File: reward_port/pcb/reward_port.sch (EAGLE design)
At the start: 27 parts

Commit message: initial routing
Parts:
- removed J3: (no value), SparkFun-Connectors:M05X2PTH
- added INDICATOR_LED: (no value), SparkFun-LED:LED-3MM-NO_SILK
- added R8: 270, SparkFun-Resistors:10KOHM-1/10W-1%(0603)0603
- R6: value 100 -> 270
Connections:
- removed net N$20: J3.7, U$6.PB7
- removed net N$22: J3.5, U$6.PB6(ADC13)
- removed net N$23: J3.3, U$6.PB5(ADC12)
- removed net N$24: J3.1, U$6.PB4(ADC11)
- removed net N$25: J3.2, U$6.PE6
- removed net N$26: J3.4, U$6.PD7(ADC10)
- removed net N$27: J3.6, U$6.PC6
- removed net N$3: J3.9, U$6.PD6(ADC9)
- new net INDICATOR_OUT: INDICATOR_LED.A, U$6.PC6
- new net N$10: U$6.PB7
- new net N$14: U$6.PD6(ADC9)
- new net N$16: INDICATOR_LED.C, R8.2
- new net N$4: U$6.PD7(ADC10)
- new net N$5: U$6.PB6(ADC13)
- net GND: now also R8.1; no longer J3.8
- net VDD: no longer J3.10
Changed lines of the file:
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@@
 <part name="C3" library="SparkFun-Capacitors" deviceset="10UF-6.3V-20%(0603)" device="" value="10uF"/>
 <part name="C4" library="SparkFun-Capacitors" deviceset="0.1UF-25V-5%(0603)" device="" value="0.1uF"/>
-<part name="J3" library="SparkFun-Connectors" deviceset="M05X2" device="PTH"/>
-<part name="R6" library="SparkFun-Resistors" deviceset="10KOHM-1/10W-1%(0603)" device="0603" value="100"/>
+<part name="R6" library="SparkFun-Resistors" deviceset="10KOHM-1/10W-1%(0603)" device="0603" value="270"/>
 <part name="GND12" library="supply1" deviceset="GND" device=""/>
 <part name="GND13" library="supply1" deviceset="GND" device=""/>
 <part name="R7" library="SparkFun-Resistors" deviceset="10KOHM-1/10W-1%(0603)" device="0603" value="100"/>
 <part name="J7" library="SparkFun-Connectors" deviceset="M04" device="POLAR"/>
+<part name="INDICATOR_LED" library="SparkFun-LED" deviceset="LED" device="-3MM-NO_SILK"/>
+<part name="R8" library="SparkFun-Resistors" deviceset="10KOHM-1/10W-1%(0603)" device="0603" value="270"/>
 <part name="GND14" library="supply1" deviceset="GND" device=""/>
 </parts>
@@
 <instance part="C3" gate="G$1" x="408.94" y="411.48"/>
 <instance part="C4" gate="G$1" x="388.62" y="411.48"/>
-<instance part="J3" gate="G$1" x="391.16" y="266.7"/>
 <instance part="R6" gate="G$1" x="469.9" y="256.54" rot="R90"/>
 <instance part="GND12" gate="1" x="469.9" y="246.38" rot="MR0"/>
@@
 <instance part="R7" gate="G$1" x="492.76" y="281.94" rot="R180"/>
 <instance part="J7" gate="G$1" x="403.86" y="368.3" rot="R180"/>
-<instance part="GND14" gate="1" x="414.02" y="264.16" rot="MR270"/>
+<instance part="INDICATOR_LED" gate="G$1" x="454.66" y="269.24"/>
+<instance part="R8" gate="G$1" x="454.66" y="256.54" rot="R90"/>
+<instance part="GND14" gate="1" x="454.66" y="246.38" rot="MR0"/>
 </instances>
 <busses>
@@
 </segment>
 <segment>
-<pinref part="J3" gate="G$1" pin="8"/>
 <pinref part="GND14" gate="1" pin="GND"/>
-<wire x1="411.48" y1="264.16" x2="398.78" y2="264.16" width="0.1524" layer="91"/>
+<pinref part="R8" gate="G$1" pin="1"/>
+<wire x1="454.66" y1="248.92" x2="454.66" y2="251.46" width="0.1524" layer="91"/>
 </segment>
 </net>
@@
 <wire x1="497.84" y1="281.94" x2="502.92" y2="281.94" width="0.1524" layer="91"/>
 <label x="505.46" y="284.48" size="1.778" layer="95"/>
-</segment>
-<segment>
-<pinref part="J3" gate="G$1" pin="10"/>
-<wire x1="398.78" y1="261.62" x2="401.32" y2="261.62" width="0.1524" layer="91"/>
-<label x="401.32" y="261.62" size="1.778" layer="95"/>
 </segment>
 </net>
@@
 <wire x1="469.9" y1="264.16" x2="469.9" y2="261.62" width="0.1524" layer="91"/>
 <pinref part="R6" gate="G$1" pin="2"/>
-</segment>
-</net>
-<net name="N$3" class="0">
+<wire x1="469.9" y1="266.7" x2="469.9" y2="264.16" width="0.1524" layer="91"/>
+</segment>
+</net>
+<net name="N$5" class="0">
+<segment>
+<pinref part="U$6" gate="G$1" pin="PB6(ADC13)"/>
+<wire x1="378.46" y1="266.7" x2="383.54" y2="266.7" width="0.1524" layer="91"/>
+</segment>
+</net>
+<net name="N$10" class="0">
+<segment>
+<pinref part="U$6" gate="G$1" pin="PB7"/>
+<wire x1="378.46" y1="264.16" x2="383.54" y2="264.16" width="0.1524" layer="91"/>
+</segment>
+</net>
+<net name="N$14" class="0">
 <segment>
 <pinref part="U$6" gate="G$1" pin="PD6(ADC9)"/>
-<pinref part="J3" gate="G$1" pin="9"/>
-<wire x1="383.54" y1="261.62" x2="378.46" y2="261.62" width="0.1524" layer="91"/>
-</segment>
-</net>
-<net name="N$20" class="0">
-<segment>
-<pinref part="U$6" gate="G$1" pin="PB7"/>
-<pinref part="J3" gate="G$1" pin="7"/>
-<wire x1="383.54" y1="264.16" x2="378.46" y2="264.16" width="0.1524" layer="91"/>
-</segment>
-</net>
-<net name="N$22" class="0">
-<segment>
-<pinref part="U$6" gate="G$1" pin="PB6(ADC13)"/>
-<pinref part="J3" gate="G$1" pin="5"/>
-<wire x1="383.54" y1="266.7" x2="378.46" y2="266.7" width="0.1524" layer="91"/>
-</segment>
-</net>
-<net name="N$23" class="0">
-<segment>
-<pinref part="U$6" gate="G$1" pin="PB5(ADC12)"/>
-<pinref part="J3" gate="G$1" pin="3"/>
-<wire x1="383.54" y1="269.24" x2="378.46" y2="269.24" width="0.1524" layer="91"/>
-</segment>
-</net>
-<net name="N$24" class="0">
-<segment>
-<pinref part="U$6" gate="G$1" pin="PB4(ADC11)"/>
-<pinref part="J3" gate="G$1" pin="1"/>
-<wire x1="383.54" y1="271.78" x2="378.46" y2="271.78" width="0.1524" layer="91"/>
-</segment>
-</net>
-<net name="N$25" class="0">
-<segment>
-<pinref part="J3" gate="G$1" pin="2"/>
-<wire x1="398.78" y1="271.78" x2="398.78" y2="274.32" width="0.1524" layer="91"/>
-<pinref part="U$6" gate="G$1" pin="PE6"/>
-<wire x1="378.46" y1="274.32" x2="398.78" y2="274.32" width="0.1524" layer="91"/>
-</segment>
-</net>
-<net name="N$26" class="0">
-<segment>
-<pinref part="J3" gate="G$1" pin="4"/>
-<wire x1="398.78" y1="269.24" x2="401.32" y2="271.78" width="0.1524" layer="91"/>
-<wire x1="401.32" y1="271.78" x2="401.32" y2="274.32" width="0.1524" layer="91"/>
-<wire x1="401.32" y1="274.32" x2="398.78" y2="276.86" width="0.1524" layer="91"/>
+<wire x1="378.46" y1="261.62" x2="383.54" y2="261.62" width="0.1524" layer="91"/>
+</segment>
+</net>
+<net name="N$4" class="0">
+<segment>
 <pinref part="U$6" gate="G$1" pin="PD7(ADC10)"/>
-<wire x1="398.78" y1="276.86" x2="378.46" y2="276.86" width="0.1524" layer="91"/>
-</segment>
-</net>
-<net name="N$27" class="0">
-<segment>
-<pinref part="J3" gate="G$1" pin="6"/>
-<wire x1="398.78" y1="266.7" x2="401.32" y2="266.7" width="0.1524" layer="91"/>
-<wire x1="401.32" y1="266.7" x2="403.86" y2="269.24" width="0.1524" layer="91"/>
-<wire x1="403.86" y1="269.24" x2="403.86" y2="276.86" width="0.1524" layer="91"/>
-<wire x1="403.86" y1="276.86" x2="401.32" y2="279.4" width="0.1524" layer="91"/>
+<wire x1="378.46" y1="276.86" x2="381" y2="276.86" width="0.1524" layer="91"/>
+</segment>
+</net>
+<net name="N$16" class="0">
+<segment>
+<pinref part="R8" gate="G$1" pin="2"/>
+<pinref part="INDICATOR_LED" gate="G$1" pin="C"/>
+<wire x1="454.66" y1="261.62" x2="454.66" y2="264.16" width="0.1524" layer="91"/>
+</segment>
+</net>
+<net name="INDICATOR_OUT" class="0">
+<segment>
+<pinref part="INDICATOR_LED" gate="G$1" pin="A"/>
+<wire x1="454.66" y1="271.78" x2="454.66" y2="274.32" width="0.1524" layer="91"/>
+<label x="454.66" y="274.32" size="1.778" layer="95" rot="R90"/>
+</segment>
+<segment>
 <pinref part="U$6" gate="G$1" pin="PC6"/>
-<wire x1="401.32" y1="279.4" x2="378.46" y2="279.4" width="0.1524" layer="91"/>
-</segment>
-</net>
+<wire x1="378.46" y1="279.4" x2="381" y2="279.4" width="0.1524" layer="91"/>
+<label x="381" y="279.4" size="1.778" layer="95"/>
+</segment>
+</net>

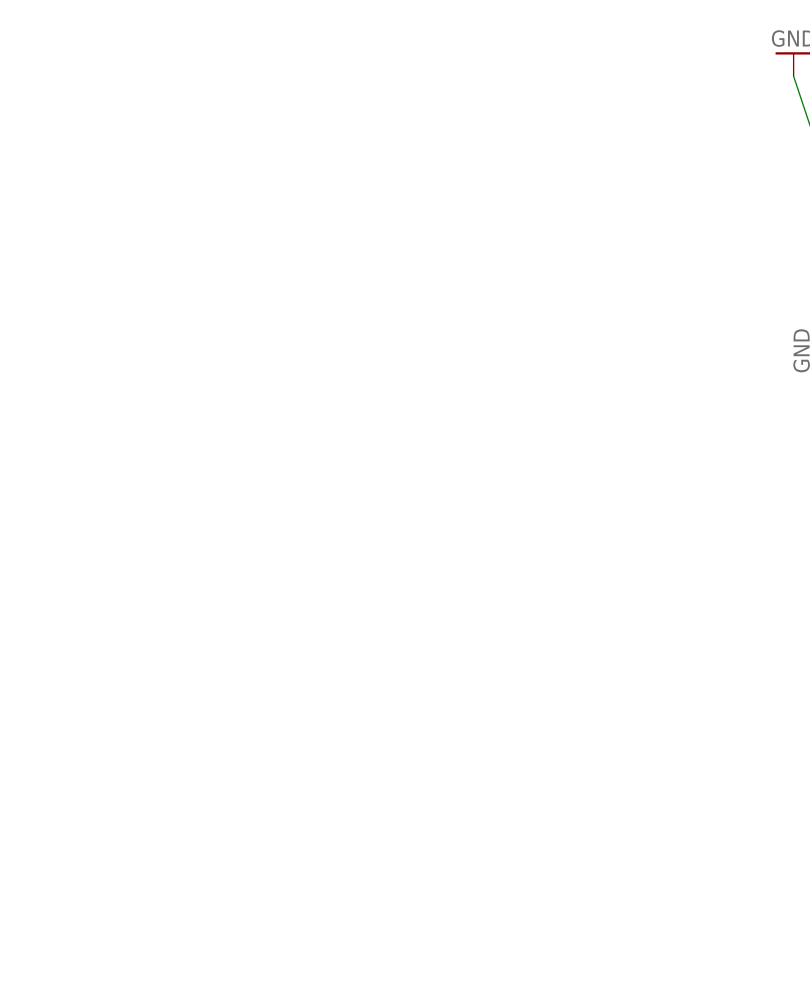
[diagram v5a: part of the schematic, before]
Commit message: test fit teensy
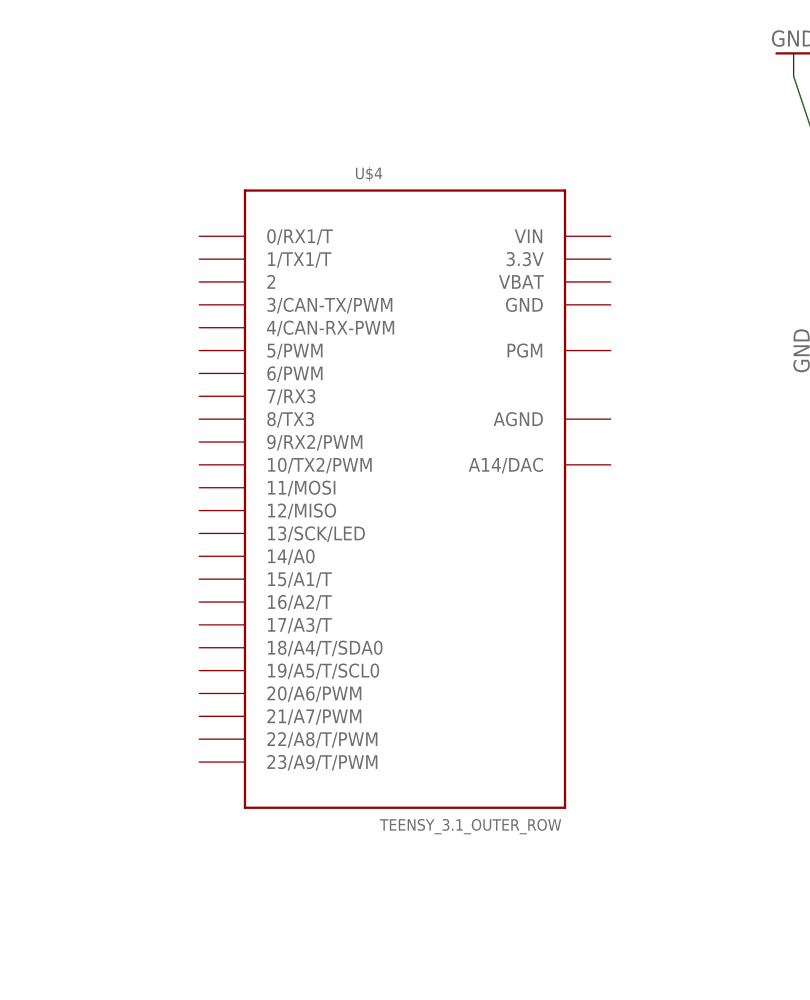
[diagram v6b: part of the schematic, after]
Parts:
- added U$4: TEENSY_3.1_OUTER_ROW, Teensy_3_and_LC_Series_Boards_v1.1:TEENSY_3.1_OUTER_ROW
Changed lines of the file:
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@@
 <setting verticaltext="up"/>
 </settings>
-<grid distance="0.1" unitdist="inch" unit="inch" style="lines" multiple="1" display="yes" altdistance="0.01" altunitdist="inch" altunit="inch"/>
+<grid distance="0.1" unitdist="inch" unit="inch" style="lines" multiple="1" display="no" altdistance="0.01" altunitdist="inch" altunit="inch"/>
 <layers>
 <layer number="1" name="Top" color="4" fill="1" visible="no" active="no"/>
@@
 <part name="R8" library="SparkFun-Resistors" deviceset="10KOHM-1/10W-1%(0603)" device="0603" value="270"/>
 <part name="GND14" library="supply1" deviceset="GND" device=""/>
+<part name="U$4" library="Teensy_3_and_LC_Series_Boards_v1.1" deviceset="TEENSY_3.1_OUTER_ROW" device=""/>
 </parts>
 <sheets>
@@
 <instance part="R8" gate="G$1" x="454.66" y="256.54" rot="R90"/>
 <instance part="GND14" gate="1" x="454.66" y="246.38" rot="MR0"/>
+<instance part="U$4" gate="G$1" x="281.94" y="287.02"/>
 </instances>
 <busses>
